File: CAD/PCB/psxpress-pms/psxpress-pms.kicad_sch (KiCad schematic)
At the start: 44 parts, among them IC1 BQ25606, IC2 MAX16054, Q1 AONR21117, SW1 SW_SPST, U1 TPS631000, U2 TPS631000, U3 MCP120-315I

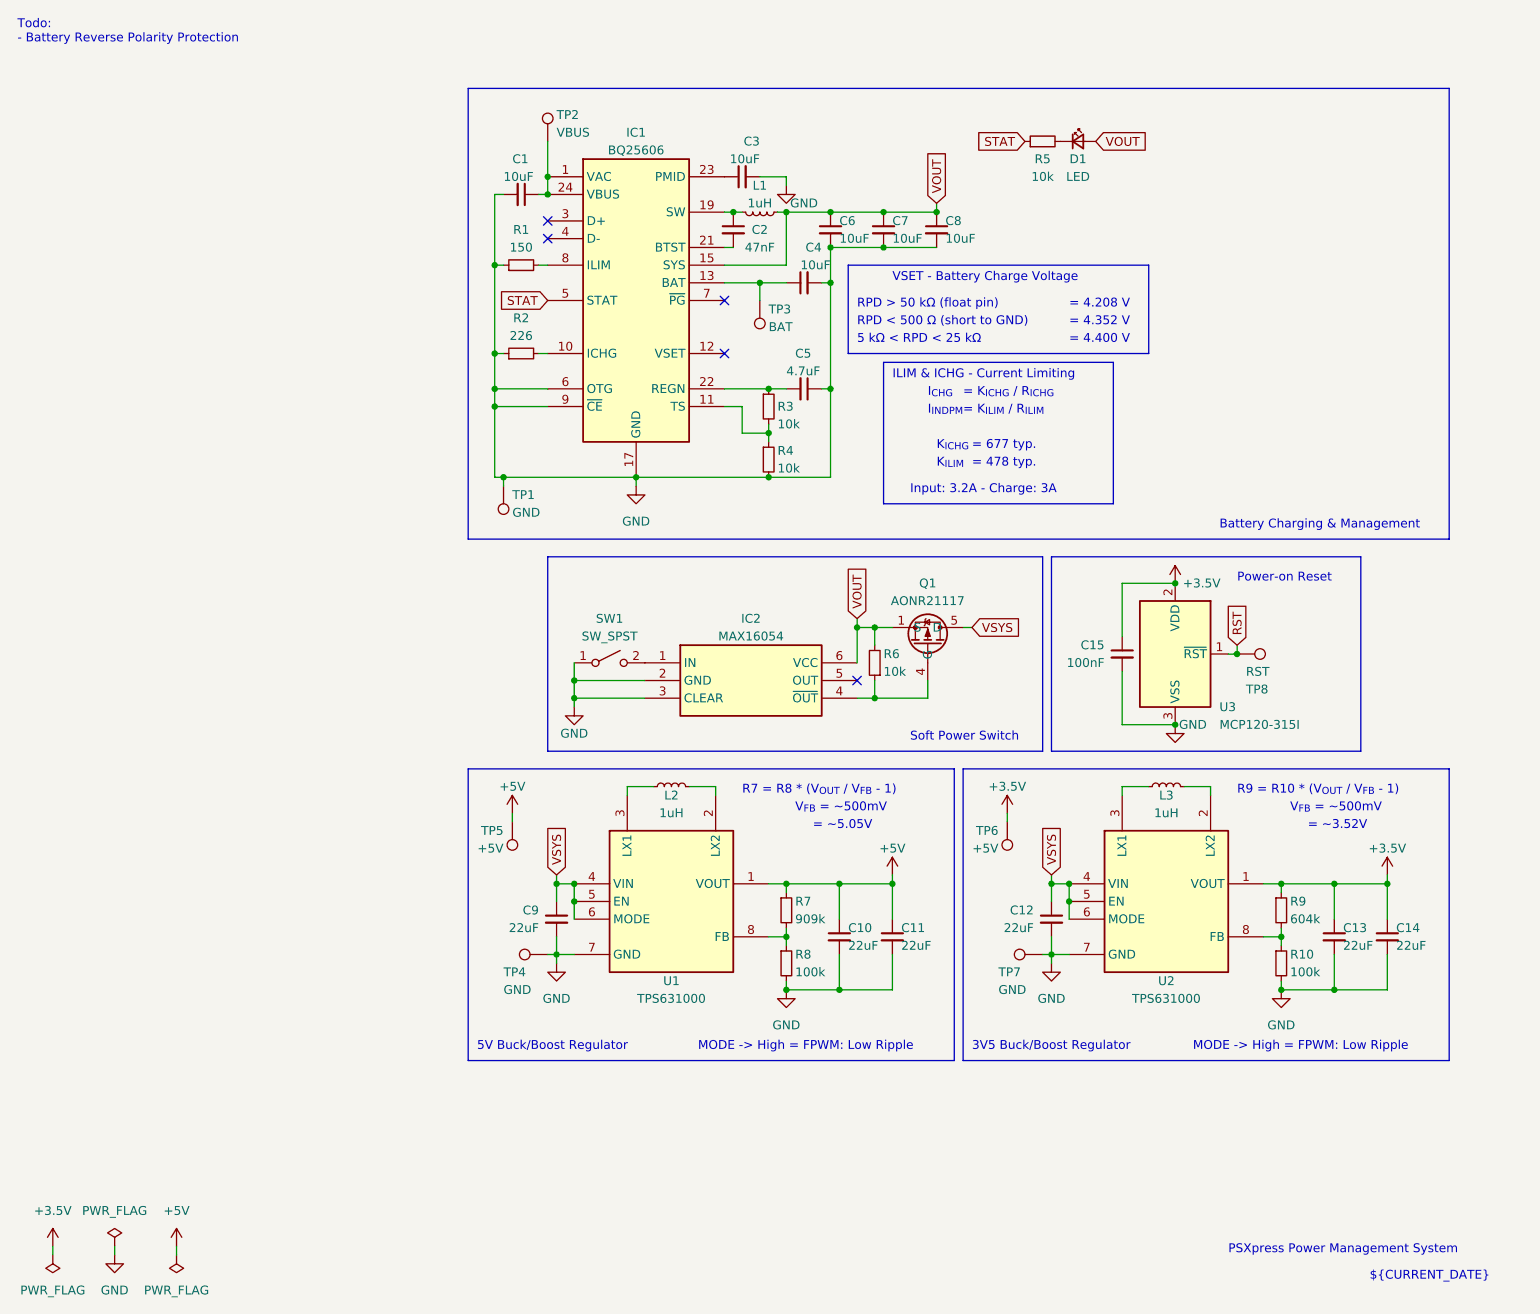
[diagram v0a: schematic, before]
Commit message: pms - add reverse polarity protection schematic
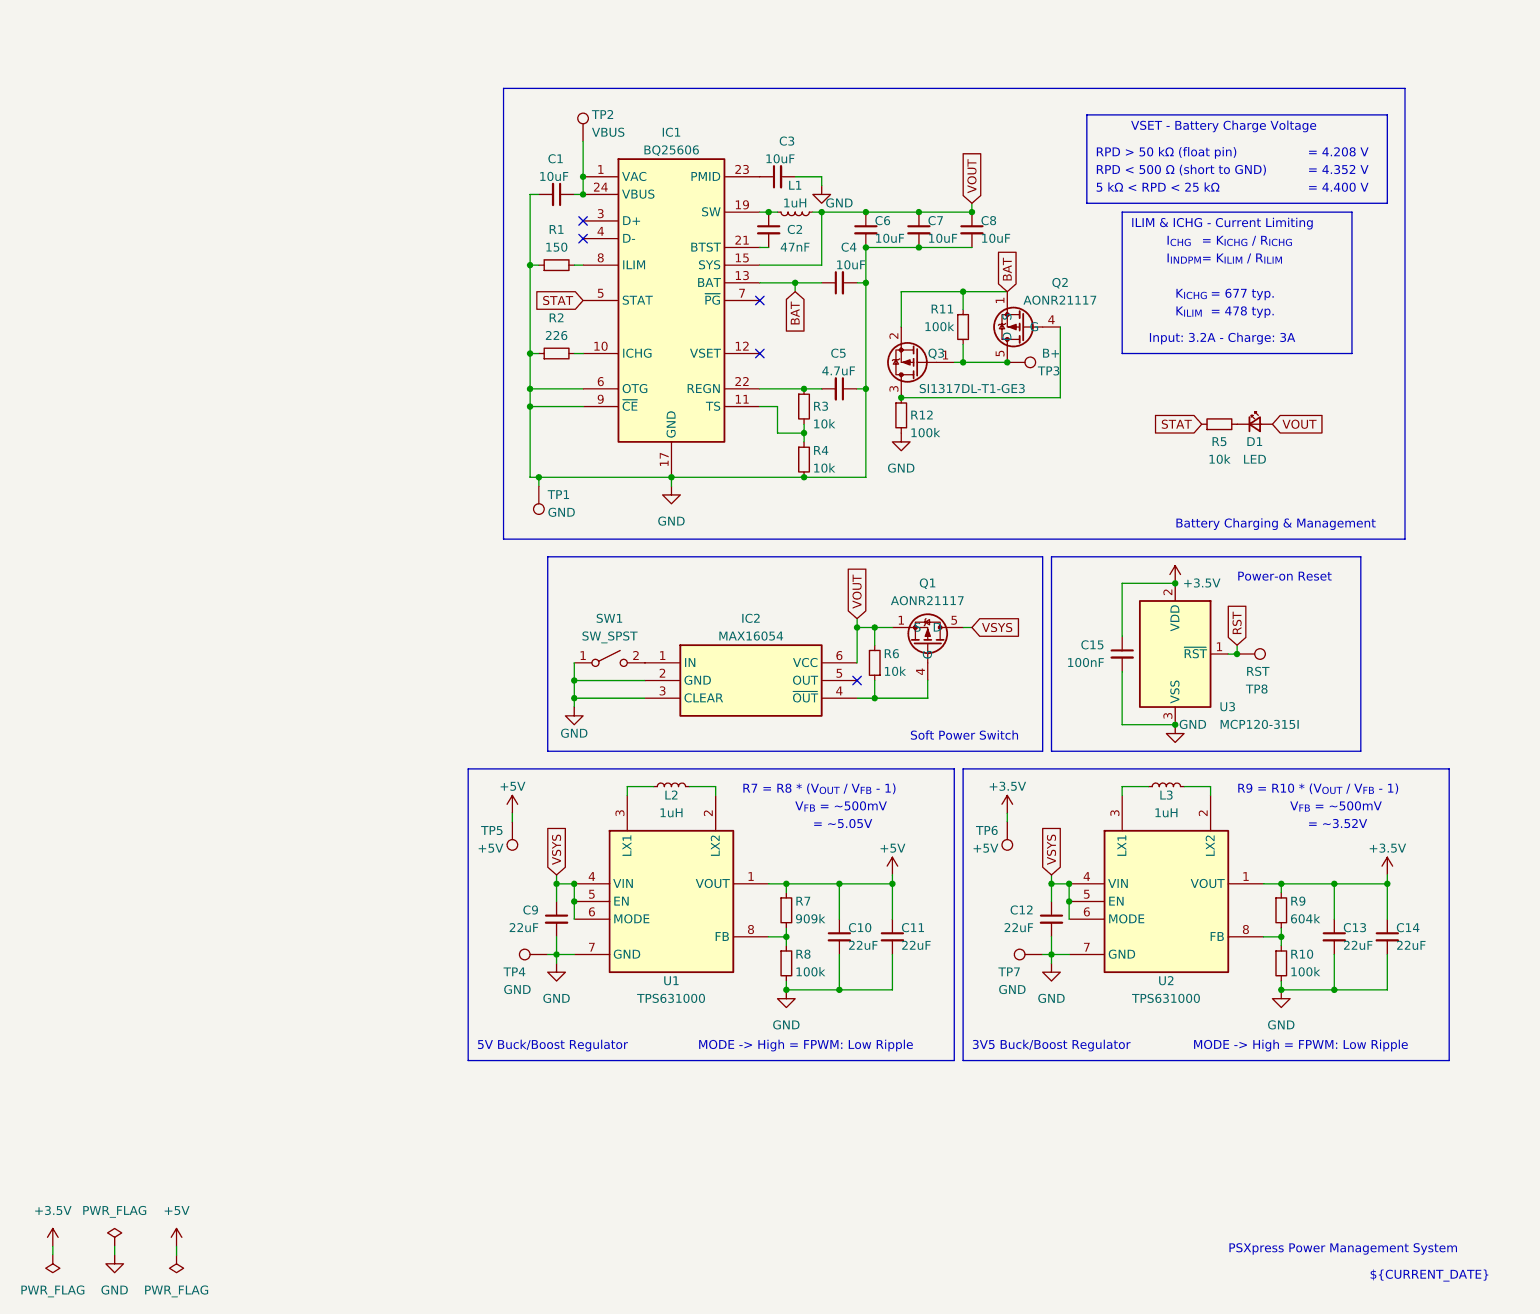
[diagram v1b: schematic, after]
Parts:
- added Q2: AONR21117, TRANS_AONR21321:TRANS_AONR21321, symbol AONR21117:AONR21117
- added Q3: SI1317DL-T1-GE3, Package_TO_SOT_SMD:SOT-323_SC-70, symbol Device:Q_PMOS_GSD
- added R11, R12: 100k, Resistor_SMD:R_0603_1608Metric, symbol Device:R_Small
- TP3: value BAT -> B+
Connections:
- net GND: now also R12.2
- net BAT: now reaches C4.1, IC1.13 (BAT), IC1.14 (BAT)
- net BAT: now also Q2.1 (S), Q2.2 (S), Q2.3 (S), Q3.2 (S), R11.1; no longer TP3.1
- new net: Q2.5 (D), Q2.6 (D), Q2.7 (D), Q2.8 (D), Q2.9 (D), Q2.9_1 (D), Q2.9_2 (D), Q3.1 (G), R11.2, TP3.1
- new net: Q2.4 (G), Q3.3 (D), R12.1
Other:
- note removed: "Todo: - Battery Reverse Polarity Protection"
- moved on the sheet: C1, C2, C3, C4, C5, C6, C7, C8, D1, IC1, L1, R1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

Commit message: pms - route reverse polarity protection circuit, finish cleanup
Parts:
- R11, R12: footprint Resistor_SMD:R_0603_1608Metric -> Resistor_SMD:R_0402_1005Metric
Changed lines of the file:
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@@
       (effects (font (size 1.27 1.27)) (justify right))
     )
-    (property "Footprint" "Resistor_SMD:R_0603_1608Metric" (at 148.59 57.15 0)
+    (property "Footprint" "Resistor_SMD:R_0402_1005Metric" (at 148.59 57.15 0)
       (effects (font (size 1.27 1.27)) hide)
     )
@@
       (effects (font (size 1.27 1.27)) (justify left))
     )
-    (property "Footprint" "Resistor_SMD:R_0603_1608Metric" (at 139.7 69.85 0)
-      (effects (font (size 1.27 1.27)) hide)
-    )
+    (property "Footprint" "Resistor_SMD:R_0402_1005Metric" (at 139.7 69.85 0)
+      (effects (font (size 1.27 1.27)) hide)
+    )

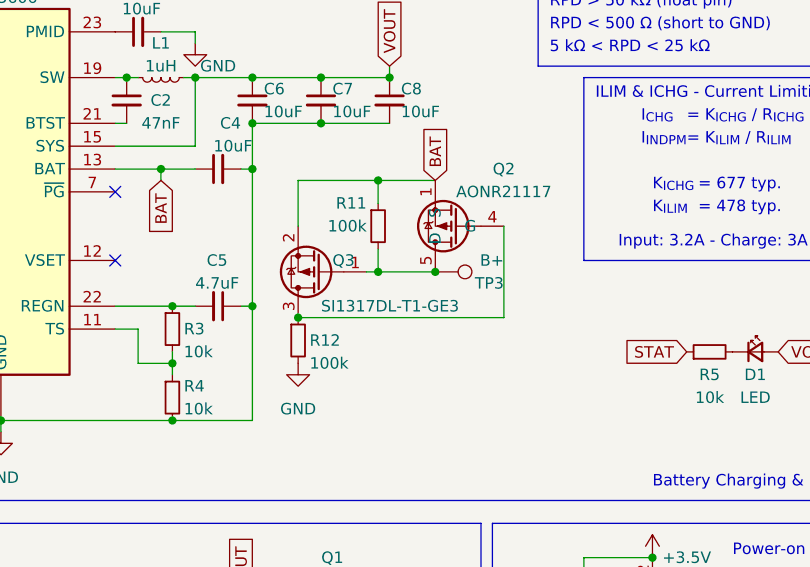
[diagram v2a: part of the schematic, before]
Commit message: pms - clear all DRC errors, further cleanup
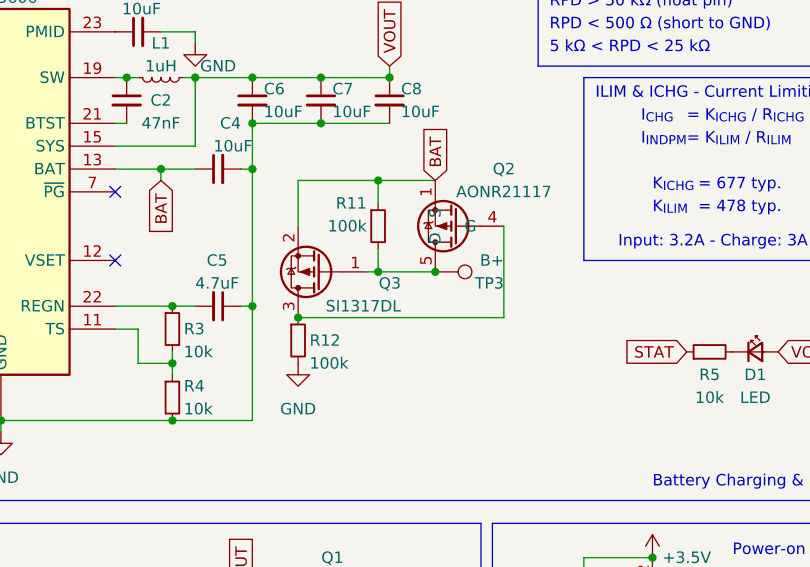
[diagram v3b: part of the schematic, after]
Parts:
- Q3: value SI1317DL-T1-GE3 -> SI1317DL
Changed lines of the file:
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@@
   (symbol (lib_id "Device:Q_PMOS_GSD") (at 142.24 62.23 180) (unit 1)
     (in_bom yes) (on_board yes) (dnp no)
-    (property "Reference" "Q3" (at 143.51 60.96 0)
-      (effects (font (size 1.27 1.27)) (justify right))
+    (property "Reference" "Q3" (at 151.13 63.5 0)
+      (effects (font (size 1.27 1.27)) (justify left))
     )
-    (property "Value" "SI1317DL-T1-GE3" (at 142.24 66.04 0)
-      (effects (font (size 1.27 1.27)) (justify right))
+    (property "Value" "SI1317DL" (at 151.13 66.04 0)
+      (effects (font (size 1.27 1.27)) (justify left))
     )
     (property "Footprint" "Package_TO_SOT_SMD:SOT-323_SC-70" (at 137.16 64.77 0)
